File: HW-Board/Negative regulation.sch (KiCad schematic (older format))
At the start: 31 parts, among them U10 AD5245, U14 INA219POS, U9 MCP4725

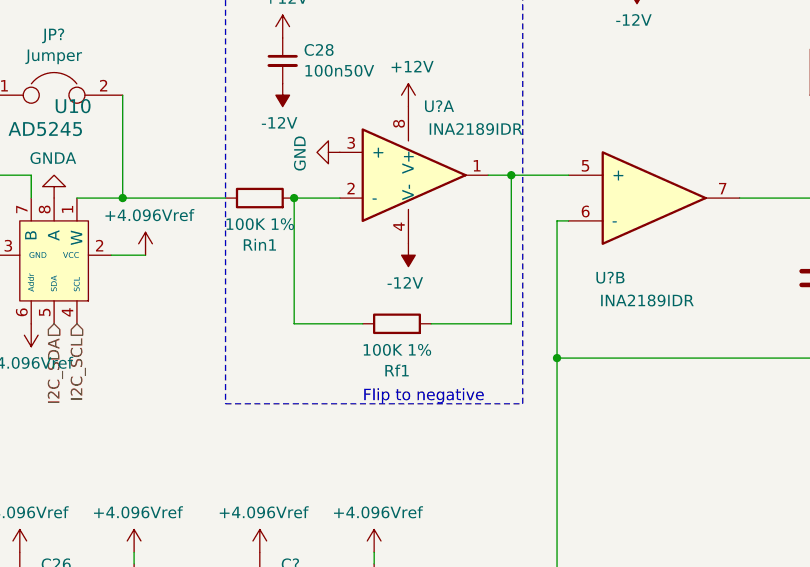
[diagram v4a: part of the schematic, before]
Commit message: Boost converter added
Go go abvoe Vgs-th at maximum output
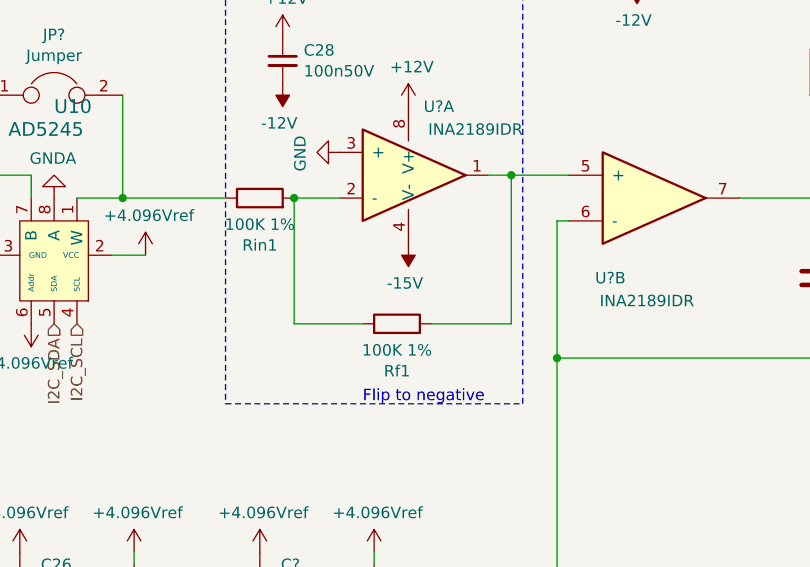
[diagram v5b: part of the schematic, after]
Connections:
- net -12V: no longer U?.4 (V-)
- new net -15V: U?.4 (V-)
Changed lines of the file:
@@
 encoding utf-8
 Sheet 4 4
-Title ""
+Title "Isolated adjustible +/- VDC PSU"
 Date "2019-05-30"
 Rev ""
@@
 $EndComp
 $Comp
-L power:-12V #PWR0189
-U 1 1 5CFDB875
-P 4450 3450
-F 0 "#PWR0189" H 4450 3550 50  0001 C CNN
-F 1 "-12V" H 4465 3623 50  0000 C CNN
-F 2 "" H 4450 3450 50  0001 C CNN
-F 3 "" H 4450 3450 50  0001 C CNN
-	1    4450 3450
-	-1   0    0    1
-$EndComp
-$Comp
 L power:GND #PWR0188
 U 1 1 5CFDAE5B
@@
 Wire Wire Line
 	6450 2150 6700 2150
+$Comp
+L power:-15V #PWR?
+U 1 1 5D668503
+P 4450 3450
+F 0 "#PWR?" H 4450 3550 50  0001 C CNN
+F 1 "-15V" H 4465 3623 50  0000 C CNN
+F 2 "" H 4450 3450 50  0001 C CNN
+F 3 "" H 4450 3450 50  0001 C CNN
+	1    4450 3450
+	-1   0    0    1
+$EndComp
 $EndSCHEMATC
